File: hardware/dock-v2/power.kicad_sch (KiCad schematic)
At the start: 0 parts

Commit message: Dock v2: all parts placed on their sheets (not wired)
149 parts across POWER, USB_PORTS, MCU_A, MCU_B, BLE and POGO (A3), in
labelled groups, with references (sheet x 100), values, footprints, LCSC
numbers (hidden LCSC field) and a Note per part. Only unconnected-pin ERC
messages remain.

5 V buck values from TI's TPS54331 Table 7-1 (5 V design), moved to Basic
parts: 12k/2.2k feedback (5.16 V), 51k + 4.7nF + 47pF compensation, 10 nF
soft start, 3 x 22 uF out; recorded in docs/dock-v2-power-input.md.
New footprint dock_v2:CP_Radial_D6.3mm_P5.00mm for the hand-soldered 220 uF.

Co-Authored-By: Claude Opus 5.5 <noreply@anthropic.com>
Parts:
- added C101: 1uF 50V, Capacitor_SMD:C_0603_1608Metric, symbol Device:C
- added C102, C103: 10uF 25V, Capacitor_SMD:C_0805_2012Metric, symbol Device:C
- added C104: 100nF, Capacitor_SMD:C_0402_1005Metric, symbol Device:C
- added C105: 10nF, Capacitor_SMD:C_0402_1005Metric, symbol Device:C
- added C106: 4.7nF, Capacitor_SMD:C_0402_1005Metric, symbol Device:C
- added C107: 47pF, Capacitor_SMD:C_0402_1005Metric, symbol Device:C
- added C108, C109, C110: 22uF 25V, Capacitor_SMD:C_1206_3216Metric, symbol Device:C
- added C111, C112: 10uF, Capacitor_SMD:C_0805_2012Metric, symbol Device:C
- added D101: SMBJ15A, Diode_SMD:D_SMB, symbol Device:D_TVS
- added D102: SS54, Diode_SMD:D_SMC, symbol Device:D_Schottky
- added H101, H102, H103, H104: MountingHole, MountingHole:MountingHole_3.2mm_M3, symbol Mechanical:MountingHole
- added J101: TYPE-C-31-M-12, Connector_USB:USB_C_Receptacle_HRO_TYPE-C-31-M-12, symbol Connector:USB_C_Receptacle_USB2.0_16P
- added L101: 6.8uH, symbol Device:L
- added R101: 6.8k, Resistor_SMD:R_0402_1005Metric, symbol Device:R
- added R102: 10k, Resistor_SMD:R_0402_1005Metric, symbol Device:R
- added R103, R104: 4.7k, Resistor_SMD:R_0402_1005Metric, symbol Device:R
- added R105: 51k, Resistor_SMD:R_0402_1005Metric, symbol Device:R
- added R106: 12k, Resistor_SMD:R_0402_1005Metric, symbol Device:R
- added R107: 2.2k, Resistor_SMD:R_0402_1005Metric, symbol Device:R
- added U101: TPD4E1U06DBVR, Package_TO_SOT_SMD:SOT-23-6, symbol dock_v2_custom:TPD4E1U06DBV
- added U102: CH224A, Package_SO:SSOP-10-1EP_3.9x4.9mm_P1mm_EP2.1x3.3mm, symbol dock_v2_custom:CH224A
- added U103: TPS54331DR, Package_SO:SOIC-8_3.9x4.9mm_P1.27mm, symbol dock_v2_custom:TPS54331DR
- added U104: AMS1117-3.3, Package_TO_SOT_SMD:SOT-223-3_TabPin2, symbol Regulator_Linear:AMS1117-3.3
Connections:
- new net: J101.A1 (GND), J101.A12 (GND), J101.B1 (GND), J101.B12 (GND)
- new net: J101.A4 (VBUS), J101.A9 (VBUS), J101.B4 (VBUS), J101.B9 (VBUS)
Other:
- note added: "3.3 V LDO"
- note added: "5 V buck TPS54331 (TI Table 7-1, 5 V)"
- note added: "Mounting holes (M3)"
- note added: "PD sink CH224A (9 V, I2C to MCU A)"
- note added: "USB-C power input (right edge)"

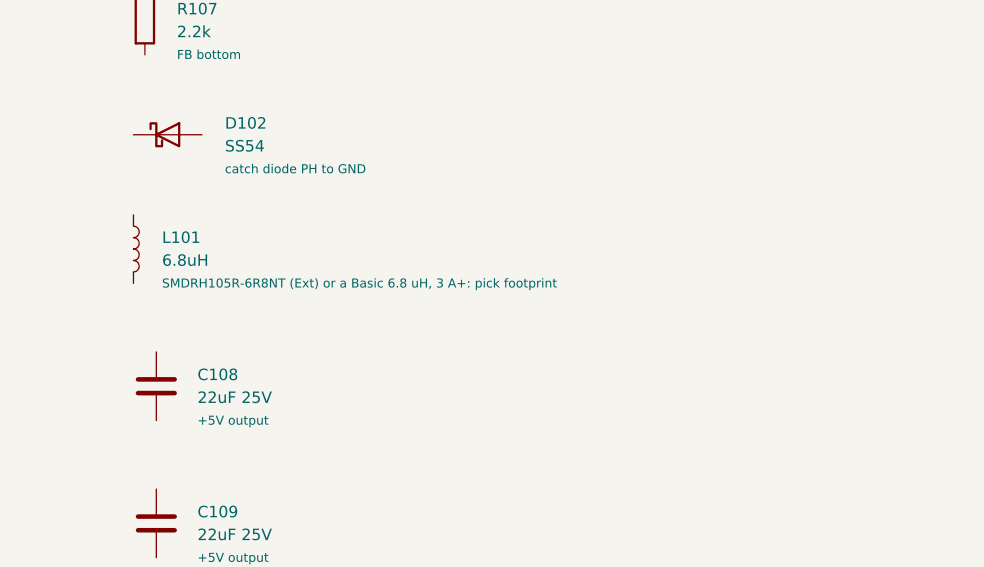
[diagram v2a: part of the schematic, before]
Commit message: Dock v2: L101 = Sunltech SLO0630H6R8MTT (6.8 uH, Isat 8 A)
JLCPCB has no Basic power inductor (only mA-rated chip inductors), so L101
is Extended either way. TPS54331 current limit is 3.5-5.8 A; SLO0630H6R8MTT
(C207841) saturates at 8 A typ, 4.5 A rated, 45 mOhm, 7.1 x 6.6 x 3.0 mm,
$0.11, 7.9k in stock. Footprint Inductor_SMD:L_TechFuse_SL0630: same body
and 3.6 mm pad gap as Sunltech's recommended land pattern.

Guide generator: read notes containing ')' and escape '|' in tables.

Co-Authored-By: Claude Opus 5.5 <noreply@anthropic.com>
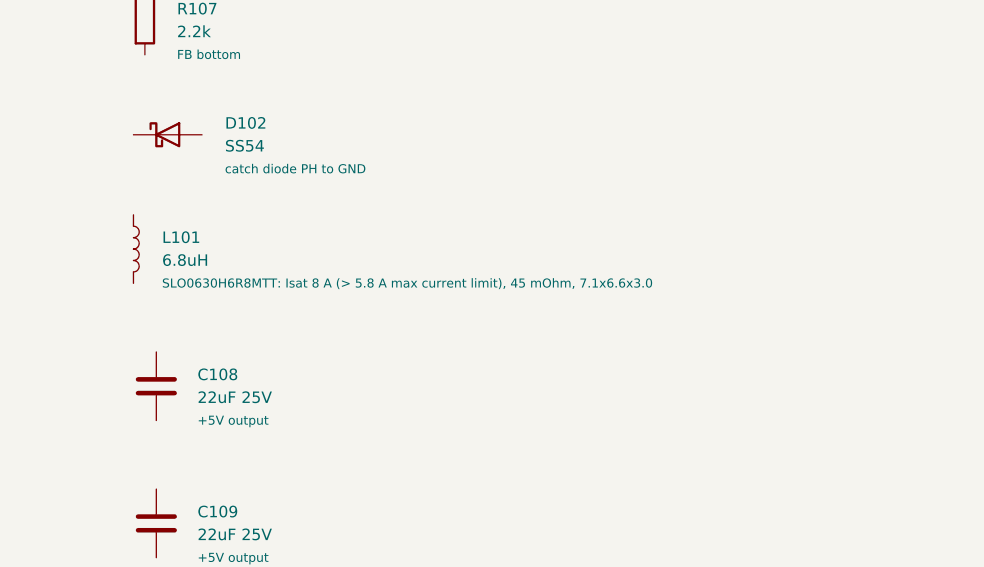
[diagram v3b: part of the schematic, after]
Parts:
- L101: footprint (none) -> Inductor_SMD:L_TechFuse_SL0630; LCSC C10167 -> C207841; Note SMDRH105R-6R8NT (Ext) or a Basic 6.8 uH, 3 A+: pick footpri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 -> SLO0630H6R8MTT: Isat 8 A (> 5.8 A max current limit), 45 mO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
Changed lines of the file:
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@@
 			)
 		)
-		(property "Footprint" ""
+		(property "Footprint" "Inductor_SMD:L_TechFuse_SL0630"
 			(at 259.08 87.63 0)
 			(hide yes)
@@
 			)
 		)
-		(property "LCSC" "C10167"
+		(property "LCSC" "C207841"
 			(at 259.08 87.63 0)
 			(hide yes)
@@
 			)
 		)
-		(property "Note" "SMDRH105R-6R8NT (Ext) or a Basic 6.8 uH, 3 A+: pick footprint"
+		(property "Note" "SLO0630H6R8MTT: Isat 8 A (> 5.8 A max current limit), 45 mOhm, 7.1x6.6x3.0"
 			(at 262.25 91.44 0)
 			(show_name no)
